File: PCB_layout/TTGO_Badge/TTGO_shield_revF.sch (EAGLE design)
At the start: 43 parts

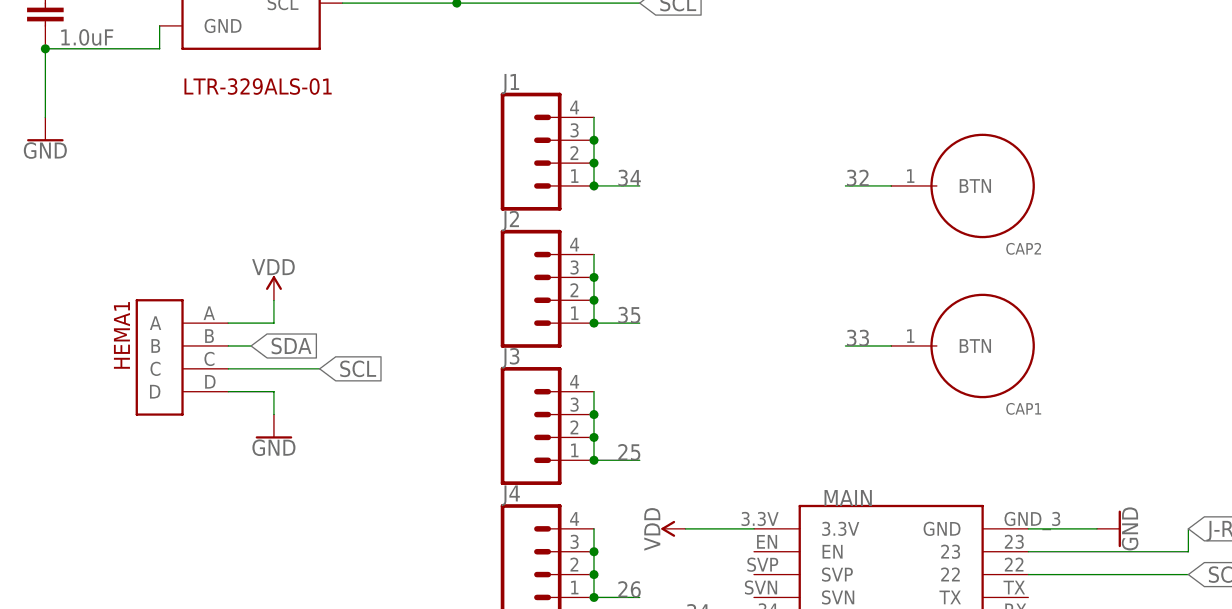
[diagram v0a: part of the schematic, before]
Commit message: round capsense buttons
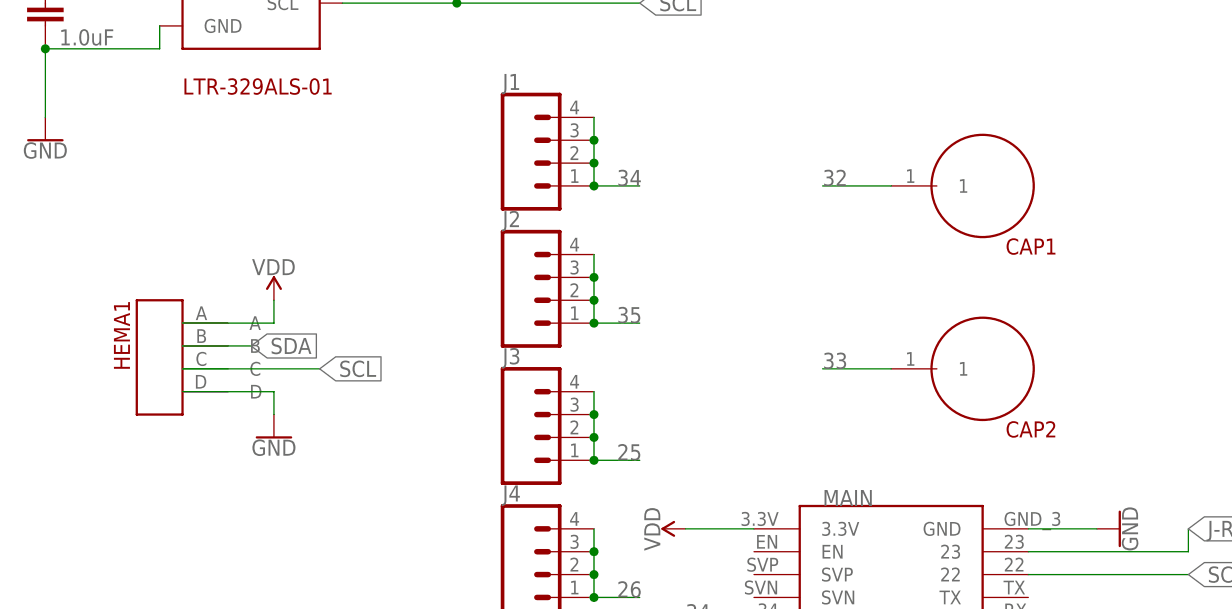
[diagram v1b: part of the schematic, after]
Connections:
- net 32: now also CAP1.1; no longer CAP2.BTN
- net 33: now also CAP2.1; no longer CAP1.BTN
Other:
- moved on the sheet: CAP1, CAP2, HEMA1
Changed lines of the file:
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@@
 <part name="J4" library="SparkFun-Connectors" library_urn="urn:adsk.eagle:library:513" deviceset="CONN_04" device="LONGPADS" package3d_urn="urn:adsk.eagle:package:38098/1"/>
 <part name="J5" library="SparkFun-Connectors" library_urn="urn:adsk.eagle:library:513" deviceset="CONN_04" device="LONGPADS" package3d_urn="urn:adsk.eagle:package:38098/1"/>
+<part name="GND5" library="SparkFun-PowerSymbols" library_urn="urn:adsk.eagle:library:530" deviceset="GND" device=""/>
 <part name="CAP1" library="BadgeParts" deviceset="CAPSENSE_BUTTON" device=""/>
 <part name="CAP2" library="BadgeParts" deviceset="CAPSENSE_BUTTON" device=""/>
-<part name="GND5" library="SparkFun-PowerSymbols" library_urn="urn:adsk.eagle:library:530" deviceset="GND" device=""/>
 </parts>
 <sheets>
@@
 <instance part="J4" gate="G$1" x="-48.26" y="43.18"/>
 <instance part="J5" gate="G$1" x="-48.26" y="27.94"/>
-<instance part="CAP1" gate="G$1" x="-5.08" y="68.58"/>
-<instance part="CAP2" gate="G$1" x="-5.08" y="86.36"/>
 <instance part="GND5" gate="1" x="63.5" y="-106.68"/>
+<instance part="CAP1" gate="G$1" x="0" y="86.36"/>
+<instance part="CAP2" gate="G$1" x="0" y="66.04"/>
 </instances>
 <busses>
@@
 <segment>
 <pinref part="HEMA1" gate="G$1" pin="A"/>
-<wire x1="-83.82" y1="71.12" x2="-78.74" y2="71.12" width="0.1524" layer="91"/>
+<wire x1="-88.9" y1="71.12" x2="-78.74" y2="71.12" width="0.1524" layer="91"/>
 <wire x1="-78.74" y1="71.12" x2="-78.74" y2="73.66" width="0.1524" layer="91"/>
 <pinref part="SUPPLY6" gate="VDD" pin="VDD"/>
@@
 <pinref part="HEMA1" gate="G$1" pin="D"/>
 <pinref part="GND6" gate="1" pin="GND"/>
-<wire x1="-83.82" y1="63.5" x2="-78.74" y2="63.5" width="0.1524" layer="91"/>
+<wire x1="-88.9" y1="63.5" x2="-78.74" y2="63.5" width="0.1524" layer="91"/>
 <wire x1="-78.74" y1="63.5" x2="-78.74" y2="60.96" width="0.1524" layer="91"/>
 </segment>
@@
 <segment>
 <pinref part="HEMA1" gate="G$1" pin="B"/>
-<wire x1="-83.82" y1="68.58" x2="-81.28" y2="68.58" width="0.1524" layer="91"/>
+<wire x1="-88.9" y1="68.58" x2="-81.28" y2="68.58" width="0.1524" layer="91"/>
 <label x="-81.28" y="68.58" size="1.778" layer="95" xref="yes"/>
 </segment>
@@
 <pinref part="HEMA1" gate="G$1" pin="C"/>
 <label x="-73.66" y="66.04" size="1.778" layer="95" xref="yes"/>
-<wire x1="-83.82" y1="66.04" x2="-73.66" y2="66.04" width="0.1524" layer="91"/>
+<wire x1="-88.9" y1="66.04" x2="-73.66" y2="66.04" width="0.1524" layer="91"/>
 </segment>
 </net>
@@
 </segment>
 <segment>
-<pinref part="CAP2" gate="G$1" pin="BTN"/>
-<wire x1="-10.16" y1="86.36" x2="-15.24" y2="86.36" width="0.1524" layer="91"/>
-<label x="-15.24" y="86.36" size="1.778" layer="95"/>
+<pinref part="CAP1" gate="G$1" pin="1"/>
+<wire x1="-10.16" y1="86.36" x2="-17.78" y2="86.36" width="0.1524" layer="91"/>
+<label x="-17.78" y="86.36" size="1.778" layer="95"/>
 </segment>
 </net>
@@
 </segment>
 <segment>
-<pinref part="CAP1" gate="G$1" pin="BTN"/>
-<wire x1="-10.16" y1="68.58" x2="-15.24" y2="68.58" width="0.1524" layer="91"/>
-<label x="-15.24" y="68.58" size="1.778" layer="95"/>
-</segment>
-</net>
+<pinref part="CAP2" gate="G$1" pin="1"/>
+<wire x1="-10.16" y1="66.04" x2="-17.78" y2="66.04" width="0.1524" layer="91"/>
+<label x="-17.78" y="66.04" size="1.778" layer="95"/>
+</segment>
+</net>
